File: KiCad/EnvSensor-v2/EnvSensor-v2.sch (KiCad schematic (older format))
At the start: 162 parts, among them J1 JTAG, J10 Conn_01x02, J2 Conn_01x02, J3 USB_B_Micro, J4 Conn_01x02, J5 Micro_SD_Card_Det, J6 Conn_01x02, J7 I2C, J8 HPMA115C0-003, J9 Conn_01x02, P1 USB_C_Plug_USB2.0, Q1 IRLML2502, Q2 Si3407DV, Q3 IRFR9024, Q4 AO6804A, SW1 SW_Push, SW2 Reset, SW3 SW_Push, SW4 SW_Push, SW5 SW_Push, SW6 Start, U1 STM32L451RCT6, U10 LTC3440, U11 MCP1826S-5.0, U12 MCP1825S-3.3, U13 ESP-12S, U2 E-Ink_Waveshare_4.2, U3 SCD30, U4 SCD40, U5 BMP280, U6 AP9101CK, U7 MCP73843-4.2, U8 BME280-Module, U9 LM2735XMF, Y1 16Hz, Y2 32768/12.5pF

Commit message: pcb updates
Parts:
- C45: value 1u -> 100n
- Q3: value IRFR9024 -> ZXMP6A16K
- R17: value R -> 3k
- R18: value R -> 10k
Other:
- note added: "Ctimer=?\nTfast_charge=Ctimer/100n * 1.5h\nTelapsed=Ctimer/100n * 3h"
- note added: "D11 - too much dropdown voltage wen charging li-ion\nreplace with mosfet?\n"
- note added: "Vmax=4.3V\nVref=3.3V\nR17+R18=4.3V/3.3V*10k\n=13k"
- note removed: "Vmax=4.3V\n"
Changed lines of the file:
@@
 P 10500 1900
 F 0 "R18" H 10570 1946 50  0000 L CNN
-F 1 "R" H 10570 1855 50  0000 L CNN
+F 1 "10k" H 10570 1855 50  0000 L CNN
 F 2 "Resistor_SMD:R_0805_2012Metric" V 10430 1900 50  0001 C CNN
 F 3 "~" H 10500 1900 50  0001 C CNN
@@
 P 10500 1500
 F 0 "R17" H 10570 1546 50  0000 L CNN
-F 1 "R" H 10570 1455 50  0000 L CNN
+F 1 "3k" H 10570 1455 50  0000 L CNN
 F 2 "Resistor_SMD:R_0805_2012Metric" V 10430 1500 50  0001 C CNN
 F 3 "~" H 10500 1500 50  0001 C CNN
@@
 P 15550 4150
 F 0 "Q3" V 15892 4150 50  0000 C CNN
-F 1 "IRFR9024" V 15801 4150 50  0000 C CNN
+F 1 "ZXMP6A16K" V 15801 4150 50  0000 C CNN
 F 2 "Package_TO_SOT_SMD:TO-252-2" H 15750 4250 50  0001 C CNN
 F 3 "~" H 15550 4150 50  0001 C CNN
@@
 P 10900 1900
 F 0 "C45" H 10950 2000 50  0000 L CNN
-F 1 "1u" H 10950 1800 50  0000 L CNN
+F 1 "100n" H 10950 1800 50  0000 L CNN
 F 2 "Capacitor_SMD:C_0805_2012Metric" H 10938 1750 50  0001 C CNN
 F 3 "~" H 10900 1900 50  0001 C CNN
@@
 Wire Wire Line
 	4600 4100 4900 4100
-Text Notes 11350 2000 0    44   ~ 0
-Vmax=4.3V\n
+Text Notes 11300 2050 0    44   ~ 0
+Vmax=4.3V\nVref=3.3V\nR17+R18=4.3V/3.3V*10k\n=13k
 Text Notes -3700 1900 0    44   ~ 0
 NO analog input at PB6/58\nAvailable inputs: 14,15,20,22
@@
 Text Notes -3700 2150 0    44   ~ 0
 U5 - BMP280 should allow to set i2c address\nby connecting SDO to either gnd or Vcc
+Text Notes 16350 5950 0    44   ~ 0
+Ctimer=?\nTfast_charge=Ctimer/100n * 1.5h\nTelapsed=Ctimer/100n * 3h
+Text Notes -3700 2350 0    44   ~ 0
+D11 - too much dropdown voltage wen charging li-ion\nreplace with mosfet?\n
 $EndSCHEMATC

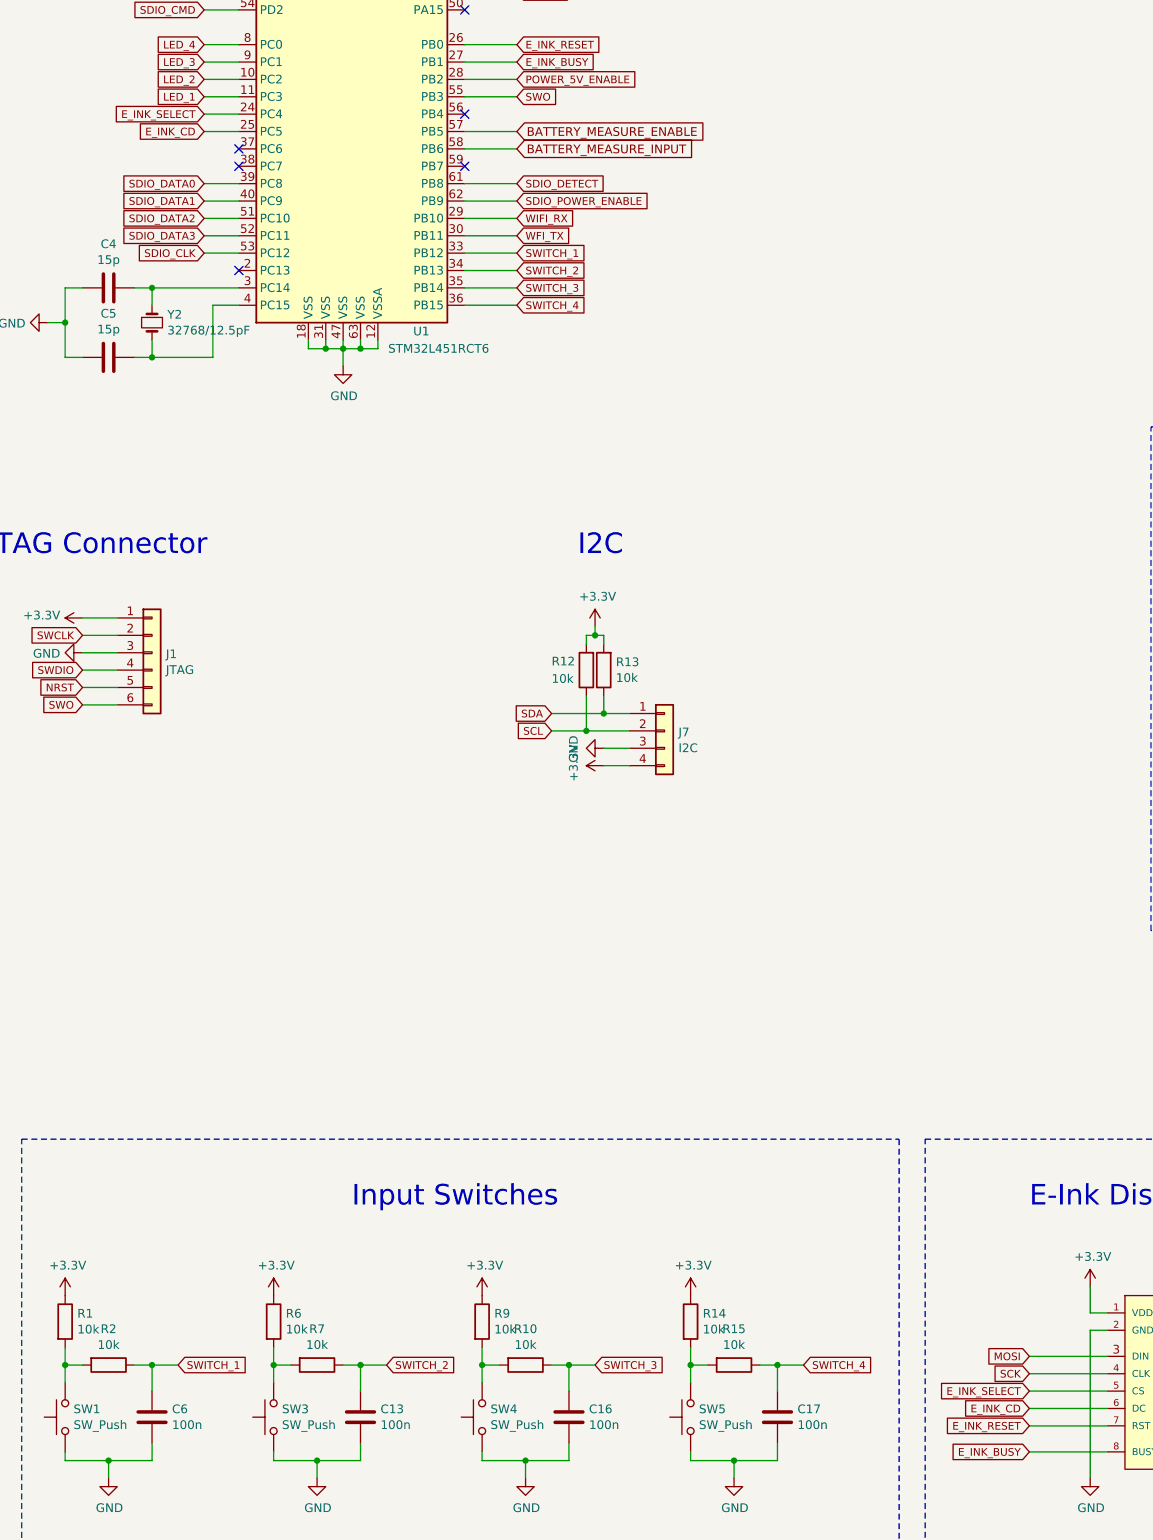
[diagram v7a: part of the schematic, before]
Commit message: touchgfx introduced
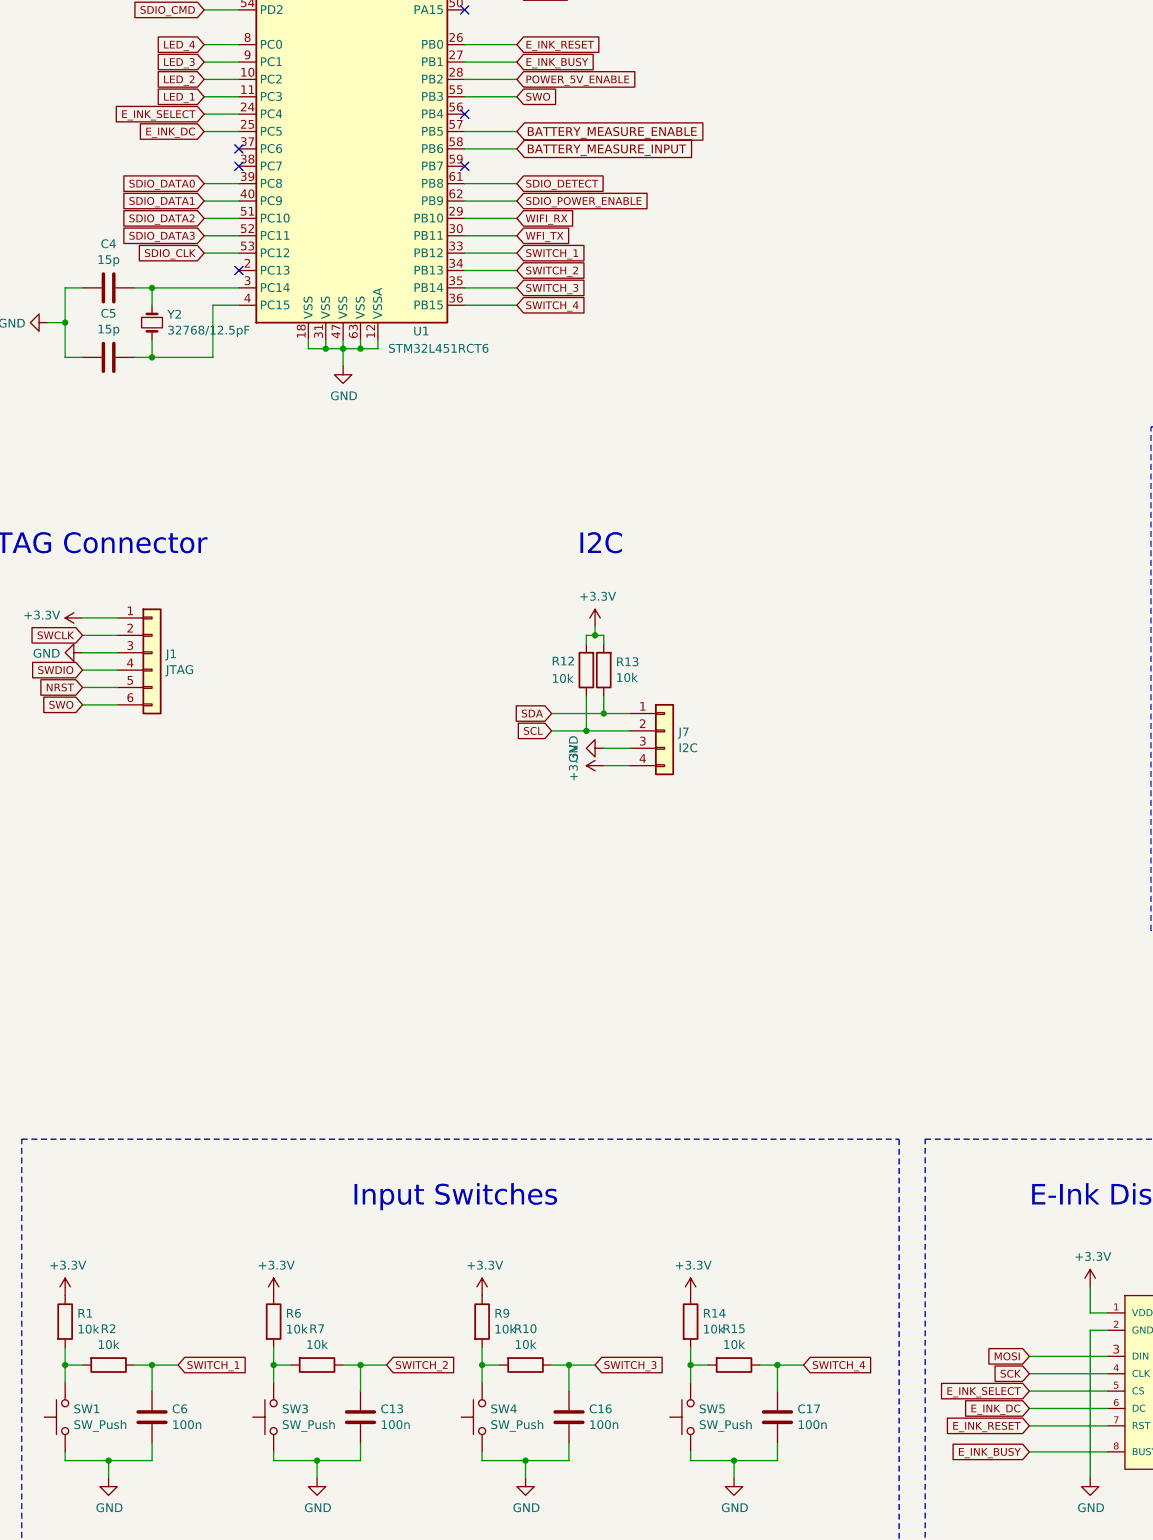
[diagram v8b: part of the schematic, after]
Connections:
- net E_INK_CD renamed E_INK_DC
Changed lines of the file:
@@
 E_INK_SELECT
 Text GLabel 7850 12450 0    44   Input ~ 0
-E_INK_CD
+E_INK_DC
 Text GLabel 7850 12550 0    44   Input ~ 0
 E_INK_RESET
@@
 E_INK_SELECT
 Text GLabel 3100 5100 0    44   Input ~ 0
-E_INK_CD
+E_INK_DC
 Text GLabel 4900 4600 2    44   Input ~ 0
 E_INK_RESET
